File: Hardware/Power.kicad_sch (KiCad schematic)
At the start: 37 parts, among them U10 INA226, U12 TPS7A4701, U14 TPS62933, U8 TPS2121RUXR

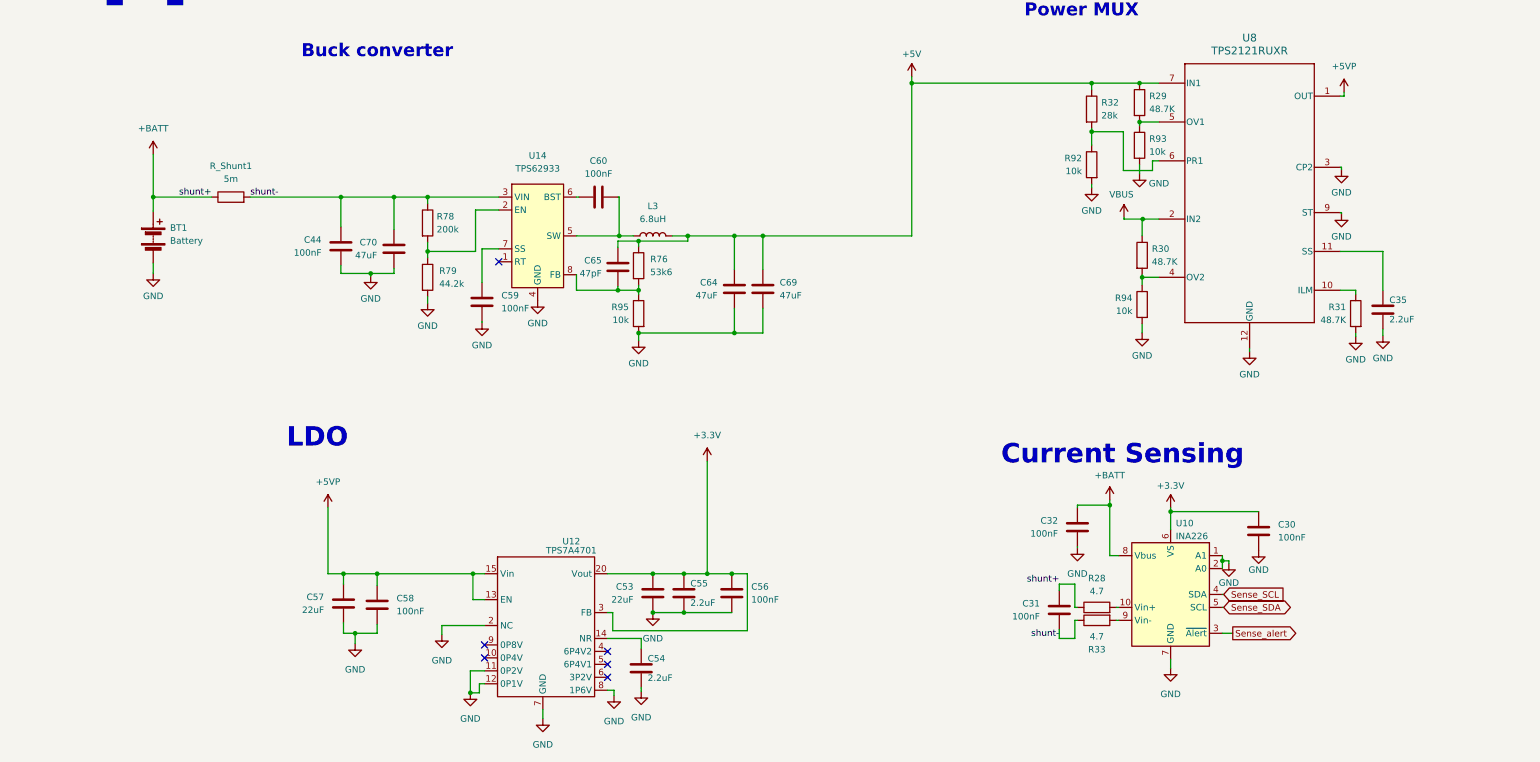
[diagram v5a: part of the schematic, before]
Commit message: Purged heavy binaries and updated gitignore
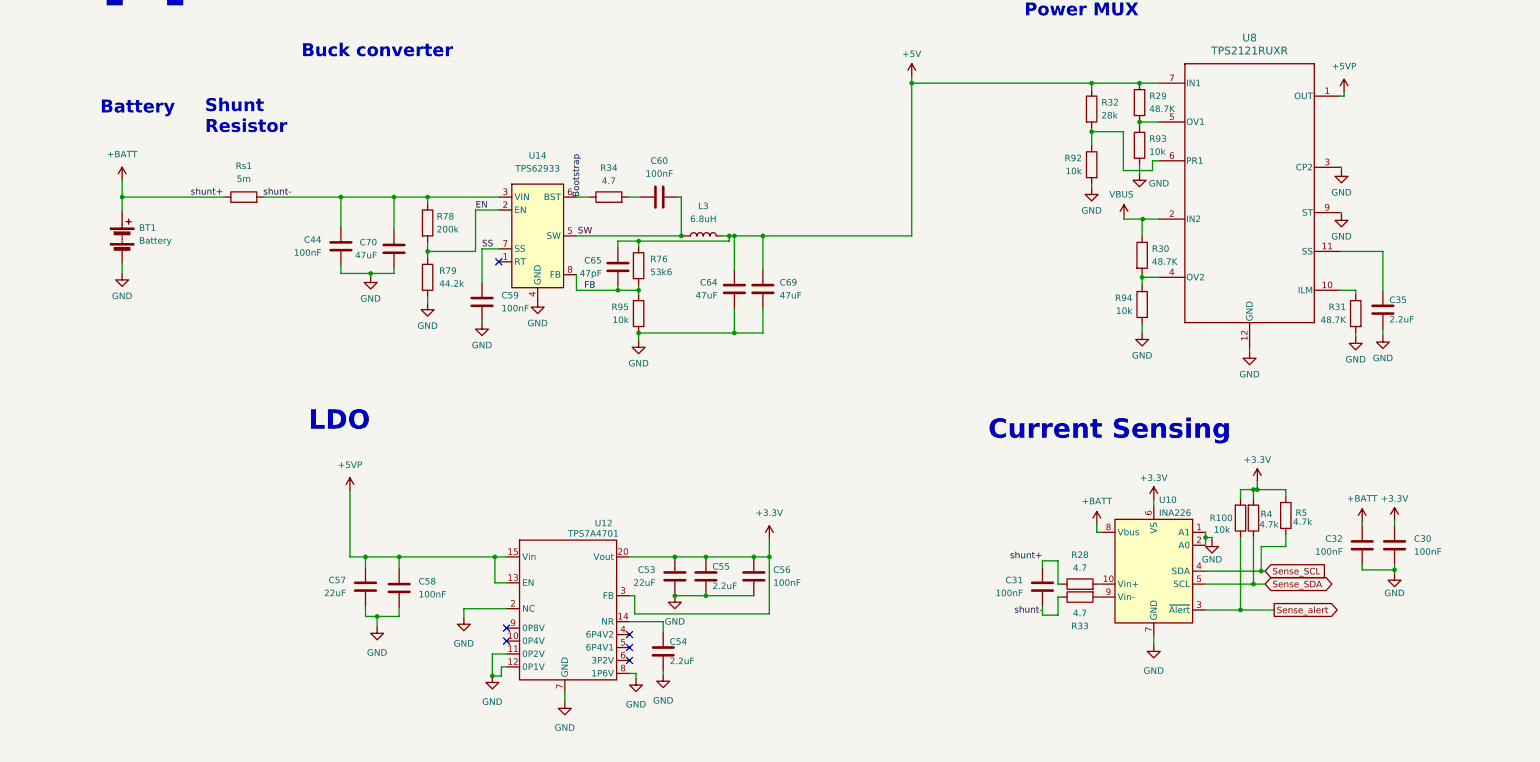
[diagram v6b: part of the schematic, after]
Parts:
- added R100: 10k, Resistor_SMD:R_0603_1608Metric, symbol Device:R
- added R34: 4.7, Resistor_SMD:R_0603_1608Metric, symbol Device:R
- added R4, R5: 4.7k, Resistor_SMD:R_0603_1608Metric, symbol Device:R
- U12: footprint Package_DFN_QFN:Texas_RGW0020A_VQFN-20-1EP_5x5mm_P0.65mm_EP3.15x3.15mm_ThermalVias -> Package_DFN_QFN:Texas_RGW0020A_VQFN-20-1EP_5x5mm_P0.65mm_EP3.15x3.15mm
- renumbered R_Shunt1 to Rs1
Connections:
- net +3.3V: now also R100.2, R4.2, R5.2
- net GND: now also U12.21 (PAD)
- net Sense_SCL: now also R5.1
- net Sense_SDA: now also R4.1
- net Sense_alert: now also R100.1
- net FB: now reaches C65.2, R76.2, R95.1, U14.8 (FB)
- net EN: now reaches R78.2, R79.1, U14.2 (EN)
- net SW: now reaches C60.2, L3.1, U14.5 (SW)
- net at C60.1: now also R34.2; no longer U14.6 (BST)
- net SS: now reaches C59.1, U14.7 (SS)
- new net Bootstrap: R34.1, U14.6 (BST)
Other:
- note added: "Battery"
- note added: "Shunt Resistor"
- moved on the sheet: BT1, C30, C31, C32, C53, C54, C55, C56, C57, C58, C60, L3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
